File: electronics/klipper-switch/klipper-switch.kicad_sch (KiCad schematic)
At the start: 0 parts

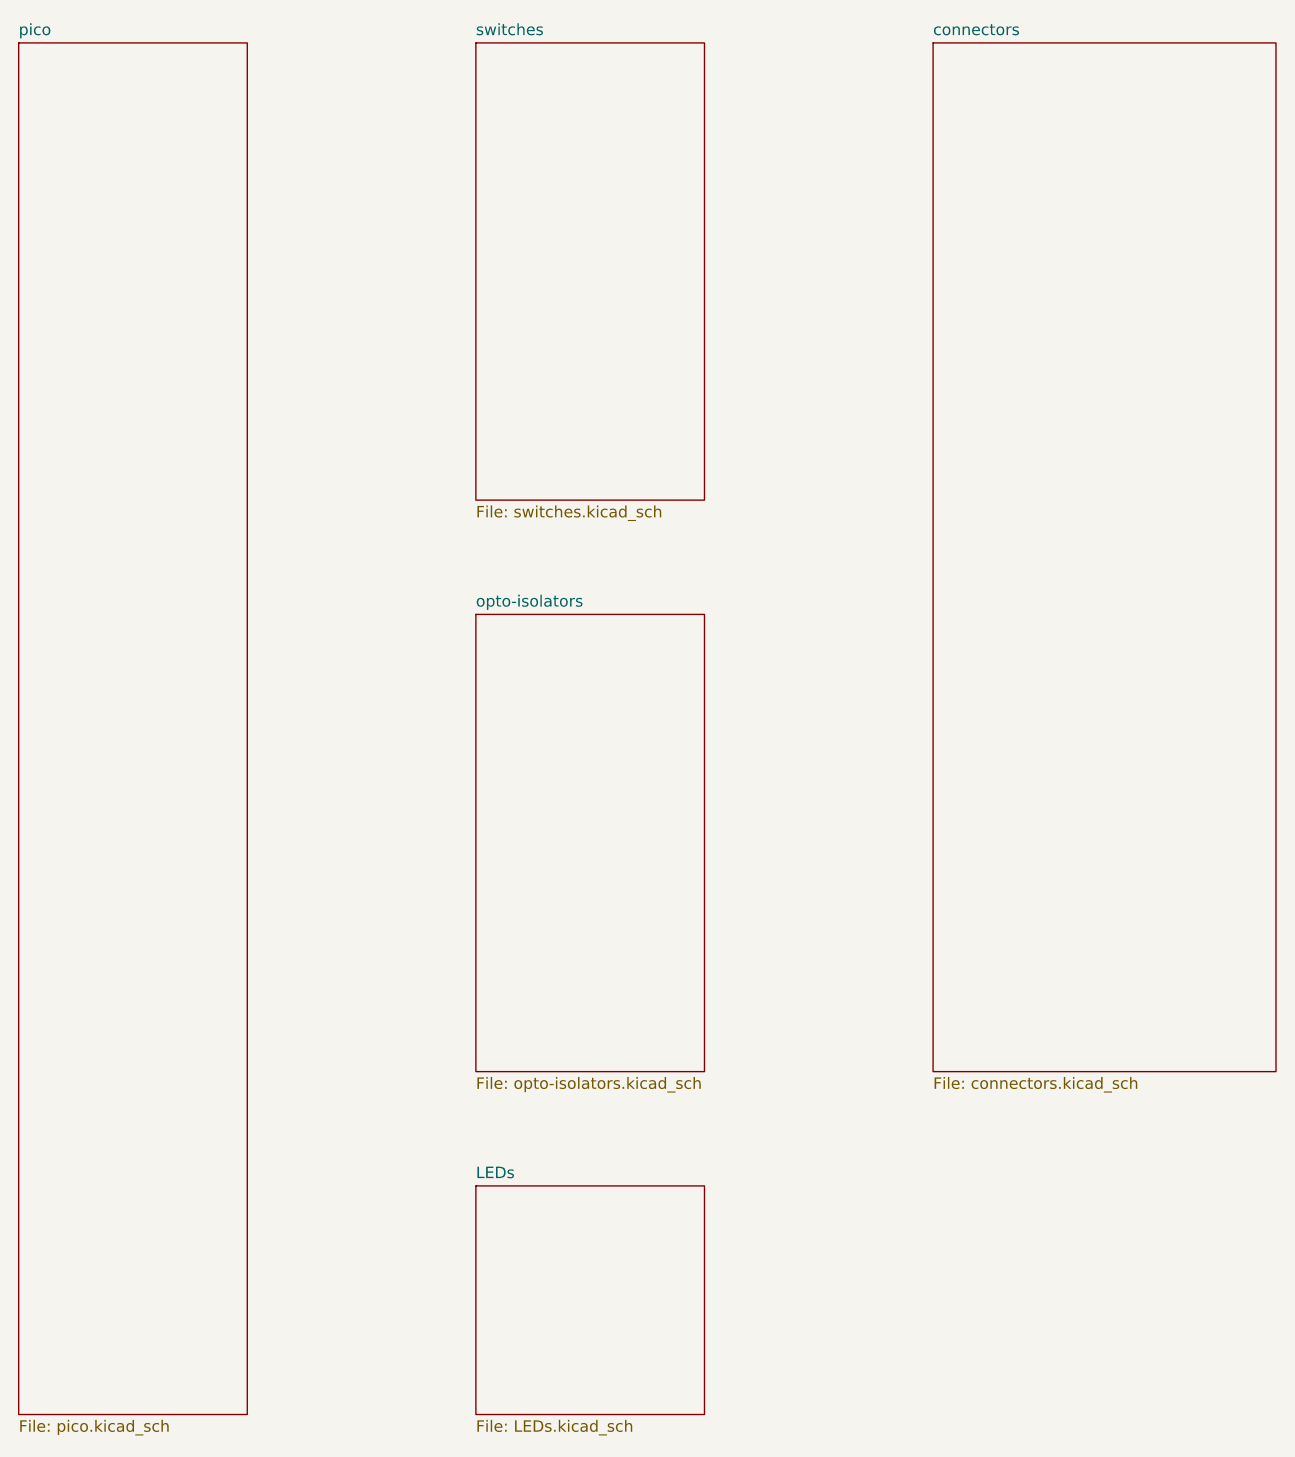
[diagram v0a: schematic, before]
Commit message: high-side switches added
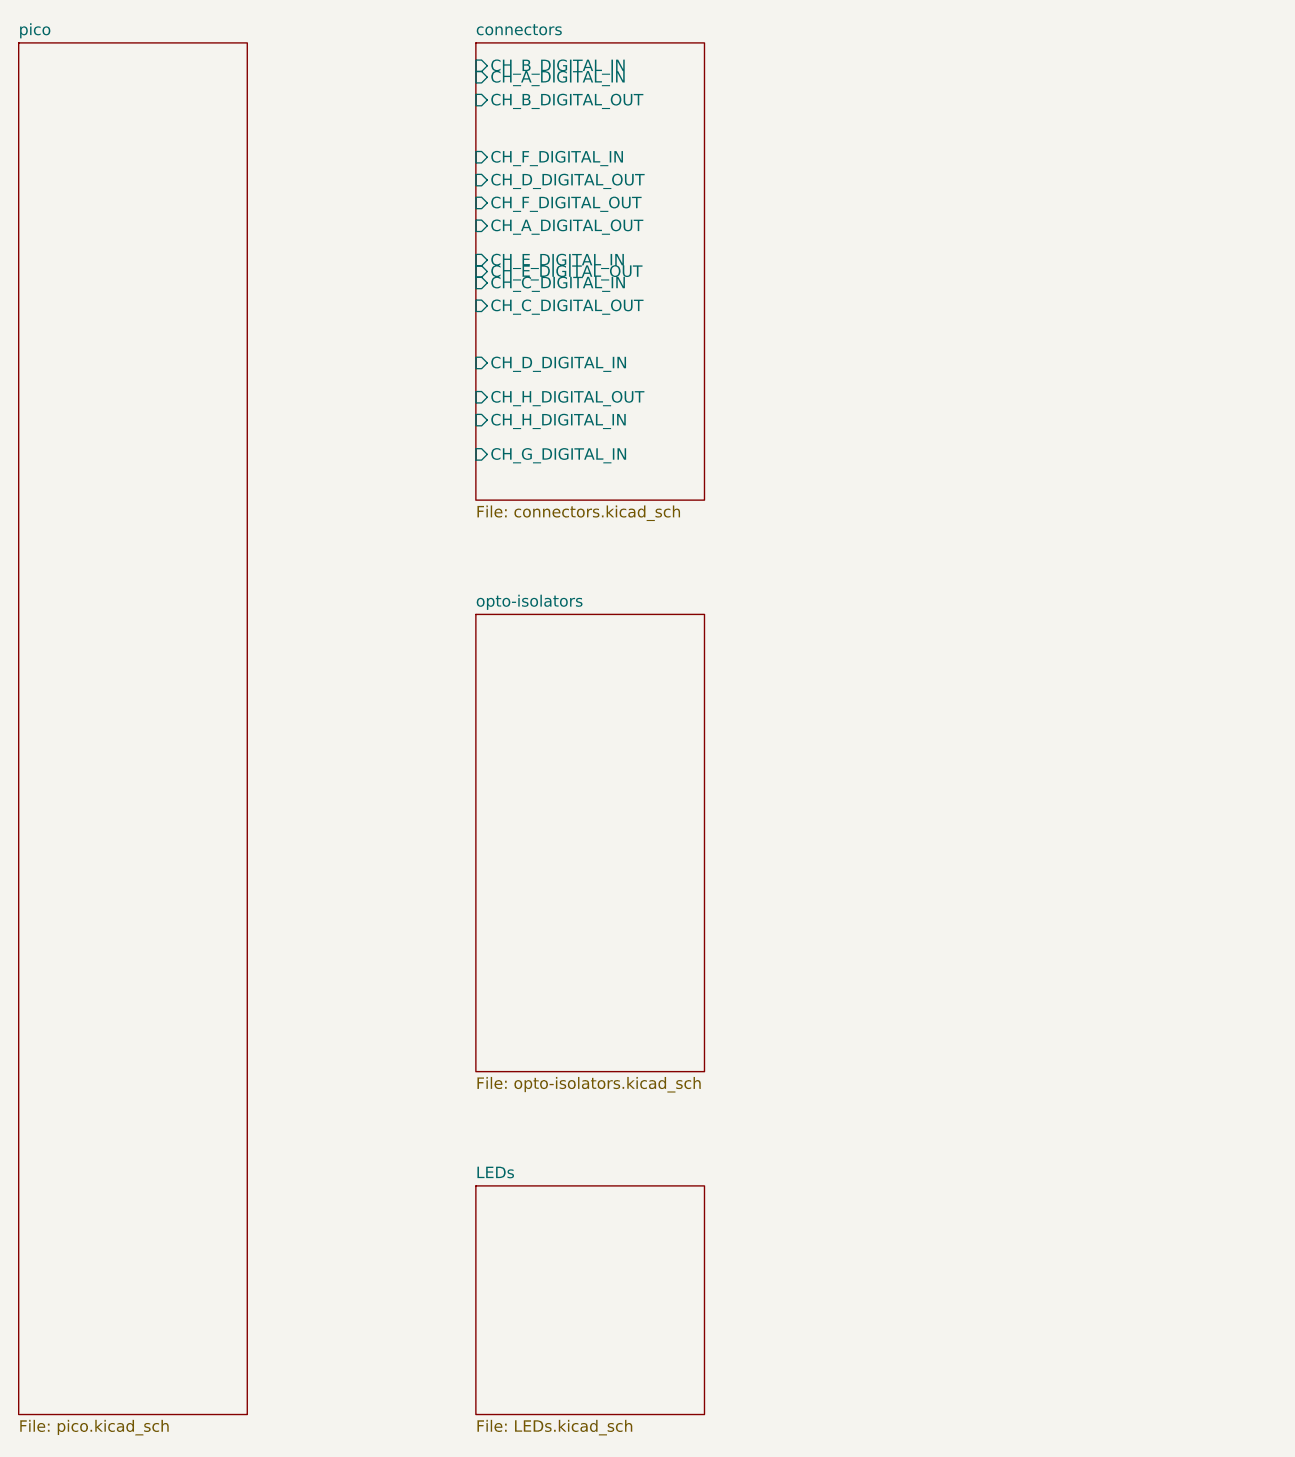
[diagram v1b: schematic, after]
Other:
- removed sheet switches
- sheet connectors ports: added CH_A_DIGITAL_IN, CH_A_DIGITAL_OUT, CH_B_DIGITAL_IN, CH_B_DIGITAL_OUT, CH_C_DIGITAL_IN, CH_C_DIGITAL_OUT, CH_D_DIGITAL_IN, CH_D_DIGITAL_OUT, CH_E_DIGITAL_IN, CH_E_DIGITAL_OUT, CH_F_DIGITAL_IN, CH_F_DIGITAL_OUT, CH_G_DIGITAL_IN, CH_H_DIGITAL_IN, CH_H_DIGITAL_OUT; removed none
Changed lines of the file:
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@@
 	)
 	(sheet
-		(at 127 25.4)
-		(size 38.1 114.3)
+		(at 76.2 25.4)
+		(size 25.4 50.8)
 		(fields_autoplaced yes)
 		(stroke
@@
 		)
 		(property "Sheetname" "connectors"
-			(at 127 24.6884 0)
+			(at 76.2 24.6884 0)
 			(effects
 				(font
@@
 		)
 		(property "Sheetfile" "connectors.kicad_sch"
-			(at 127 140.2846 0)
+			(at 76.2 76.7846 0)
 			(effects
 				(font
@@
 				)
 				(justify left top)
+			)
+		)
+		(pin "CH_E_DIGITAL_OUT" input
+			(at 76.2 50.8 180)
+			(effects
+				(font
+					(size 1.27 1.27)
+				)
+				(justify left)
+			)
+		)
+		(pin "CH_E_DIGITAL_IN" input
+			(at 76.2 49.53 180)
+			(effects
+				(font
+					(size 1.27 1.27)
+				)
+				(justify left)
+			)
+		)
+		(pin "CH_A_DIGITAL_OUT" input
+			(at 76.2 45.72 180)
+			(effects
+				(font
+					(size 1.27 1.27)
+				)
+				(justify left)
+			)
+		)
+		(pin "CH_F_DIGITAL_OUT" input
+			(at 76.2 43.18 180)
+			(effects
+				(font
+					(size 1.27 1.27)
+				)
+				(justify left)
+			)
+		)
+		(pin "CH_B_DIGITAL_OUT" input
+			(at 76.2 31.75 180)
+			(effects
+				(font
+					(size 1.27 1.27)
+				)
+				(justify left)
+			)
+		)
+		(pin "CH_B_DIGITAL_IN" input
+			(at 76.2 27.94 180)
+			(effects
+				(font
+					(size 1.27 1.27)
+				)
+				(justify left)
+			)
+		)
+		(pin "CH_A_DIGITAL_IN" input
+			(at 76.2 29.21 180)
+			(effects
+				(font
+					(size 1.27 1.27)
+				)
+				(justify left)
+			)
+		)
+		(pin "CH_F_DIGITAL_IN" input
+			(at 76.2 38.1 180)
+			(effects
+				(font
+					(size 1.27 1.27)
+				)
+				(justify left)
+			)
+		)
+		(pin "CH_D_DIGITAL_OUT" input
+			(at 76.2 40.64 180)
+			(effects
+				(font
+					(size 1.27 1.27)
+				)
+				(justify left)
+			)
+		)
+		(pin "CH_C_DIGITAL_IN" input
+			(at 76.2 52.07 180)
+			(effects
+				(font
+					(size 1.27 1.27)
+				)
+				(justify left)
+			)
+		)
+		(pin "CH_C_DIGITAL_OUT" input
+			(at 76.2 54.61 180)
+			(effects
+				(font
+					(size 1.27 1.27)
+				)
+				(justify left)
+			)
+		)
+		(pin "CH_G_DIGITAL_IN" input
+			(at 76.2 71.12 180)
+			(effects
+				(font
+					(size 1.27 1.27)
+				)
+				(justify left)
+			)
+		)
+		(pin "CH_H_DIGITAL_OUT" input
+			(at 76.2 64.77 180)
+			(effects
+				(font
+					(size 1.27 1.27)
+				)
+				(justify left)
+			)
+		)
+		(pin "CH_D_DIGITAL_IN" input
+			(at 76.2 60.96 180)
+			(effects
+				(font
+					(size 1.27 1.27)
+				)
+				(justify left)
+			)
+		)
+		(pin "CH_H_DIGITAL_IN" input
+			(at 76.2 67.31 180)
+			(effects
+				(font
+					(size 1.27 1.27)
+				)
+				(justify left)
 			)
 		)
@@
 				)
 			)
-		)
-	)
-	(sheet
-		(at 76.2 25.4)
-		(size 25.4 50.8)
-		(fields_autoplaced yes)
-		(stroke
-			(width 0.1524)
-			(type solid)
-		)
-		(fill
-			(color 0 0 0 0.0000)
-		)
-		(property "Sheetname" "switches"
-			(at 76.2 24.6884 0)
-			(effects
-				(font
-					(size 1.27 1.27)
-				)
-				(justify left bottom)
-			)
-		)
-		(property "Sheetfile" "switches.kicad_sch"
-			(at 76.2 76.7846 0)
-			(effects
-				(font
-					(size 1.27 1.27)
-				)
-				(justify left top)
-			)
-		)
-		(instances
-			(project "klipper-switch"
-				(path "/e5df92b1-e048-41e8-96e5-ed9a12dbef0e"
-					(page "3")
-				)
-			)
